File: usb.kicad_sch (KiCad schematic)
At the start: 11 parts, among them J7 USB-A_USB-303WSD-BRY, U1 AP22615AWU-7

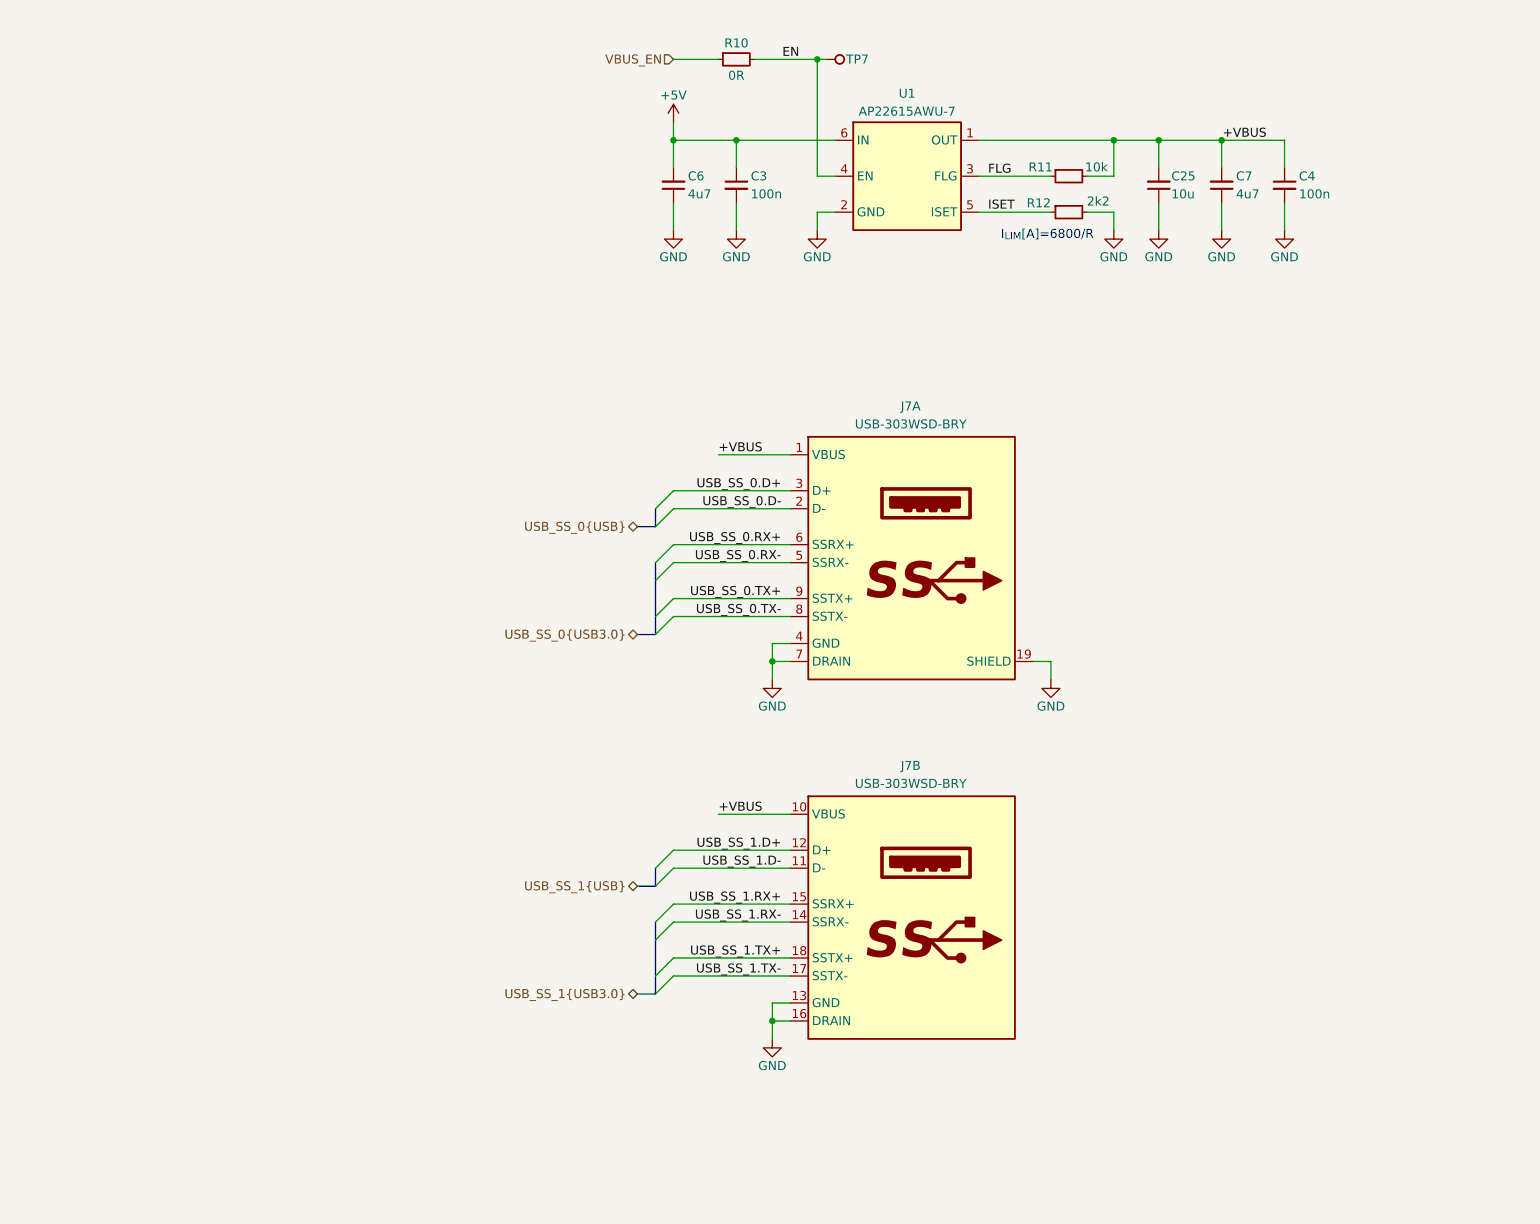
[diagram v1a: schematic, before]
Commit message: [#1] Add USB switch and 0R to USB hub data lines, minor schematic refactor
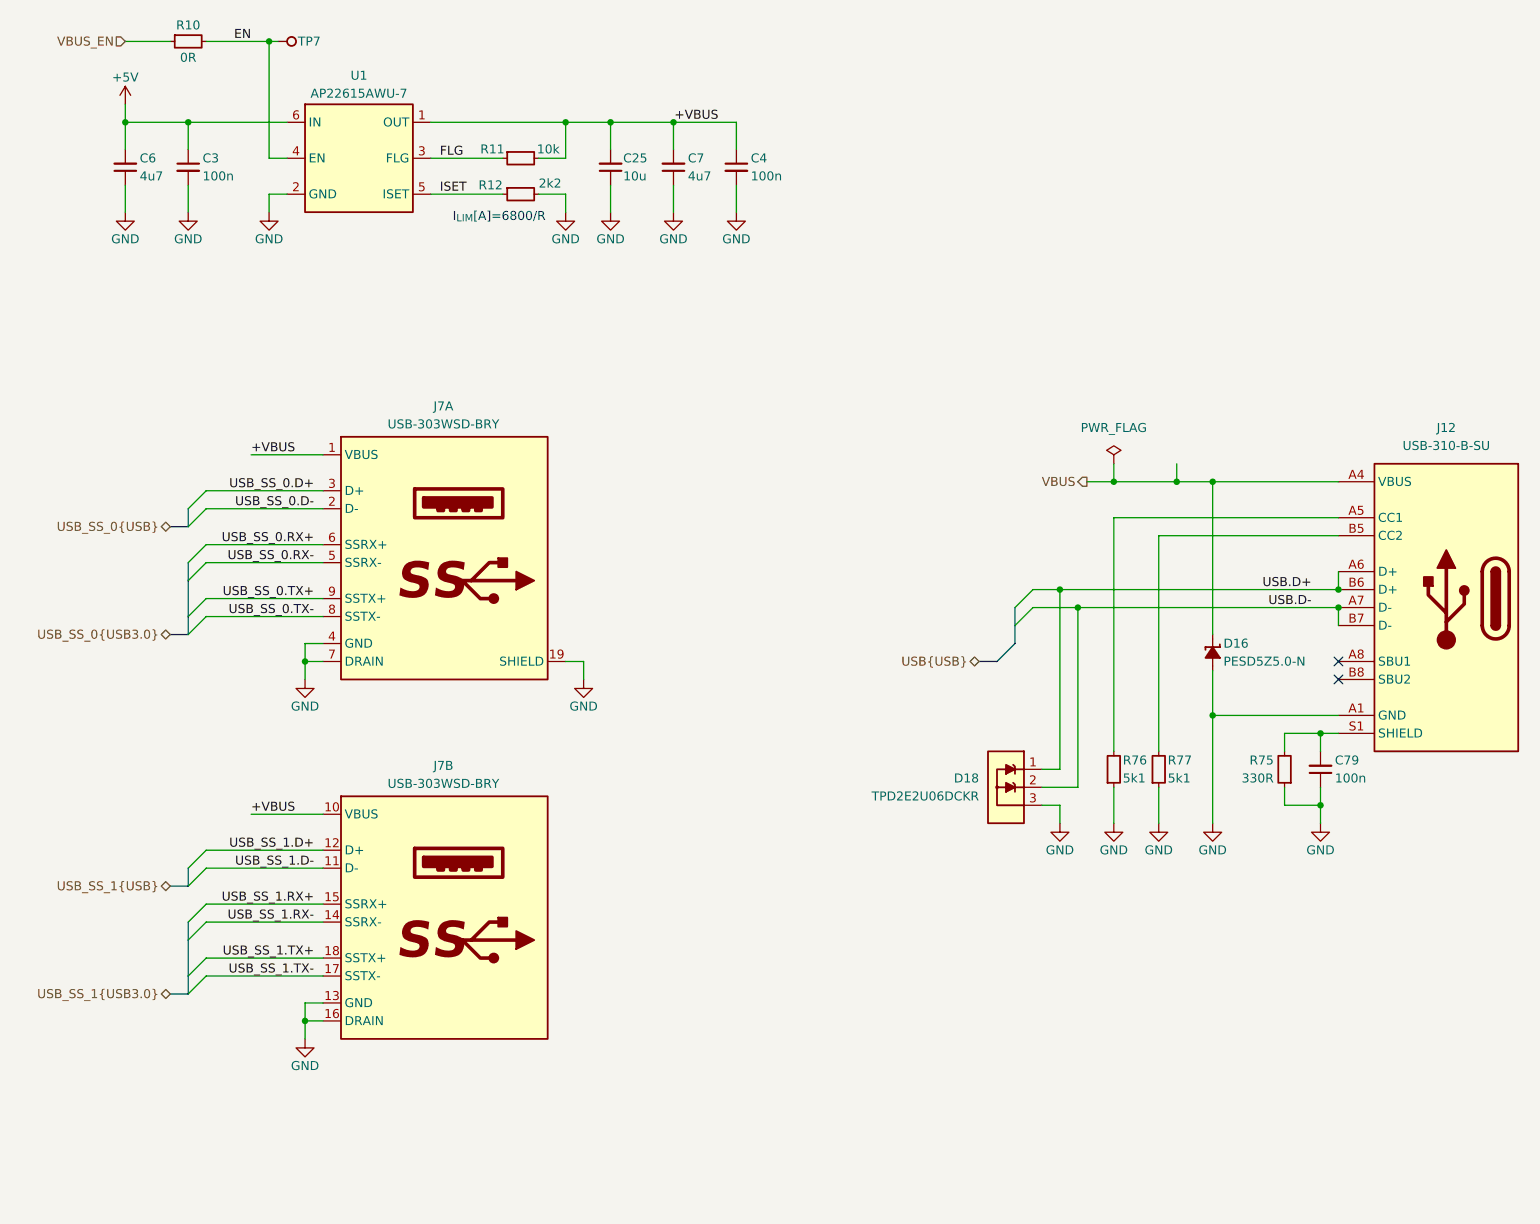
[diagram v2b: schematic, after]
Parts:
- added C79: C-100n-0402, DW-footprints:C_0402_1005Metric, symbol DW-capacitors:C-100n-0402
- added D16: PESD5Z5, DW-footprints:D_SOD-523, symbol DW-TVS:PESD5Z5
- added D18: TPD2E2U06DCKR, DW-footprints:SOT-323, symbol DW-TVS:TPD2E2U06DCKR
- added J12: USB-C_USB-310F-B-SU, DW-footprints:USB-C-Receptacle_USB-310-B-SU, symbol DW-connectors:USB-C_USB-310-B-SU
- added R75: R-330r-0402, DW-footprints:R_0402_1005Metric, symbol DW-resistors:R-330r-0402
- added R76, R77: R-5k1-0402, DW-footprints:R_0402_1005Metric, symbol DW-resistors:R-5k1-0402
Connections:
- net GND: now also C79.1, D16.2 (A), D18.3, J12.A1 (GND), J12.A12 (GND), J12.B1 (GND), J12.B12 (GND), R75.1, R76.1, R77.1
- new net: J12.A5 (CC1), R76.2
- new net: C79.2, J12.S1 (SHIELD), R75.2
- new net: J12.B5 (CC2), R77.2
- new net USB.D+: D18.1, J12.A6 (D+), J12.B6 (D+)
- new net USB.D-: D18.2, J12.A7 (D-), J12.B7 (D-)
- new net VBUS: D16.1 (C), J12.A4 (VBUS), J12.A9 (VBUS), J12.B4 (VBUS), J12.B9 (VBUS)
- no-connect marks 0 -> 2
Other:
- moved on the sheet: C25, C3, C4, C6, C7, J7A, J7B, R10, R11, R12, TP7, U1

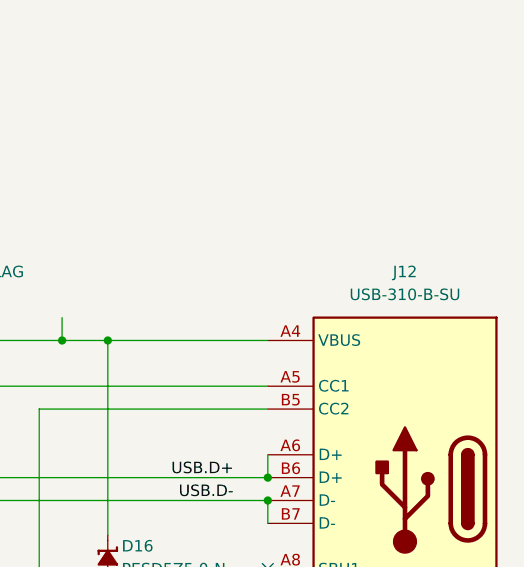
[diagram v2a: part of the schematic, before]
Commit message: [#3] Fix 3V3 DC-DC converter schematic, change one USB-C to a vertical one, start layout
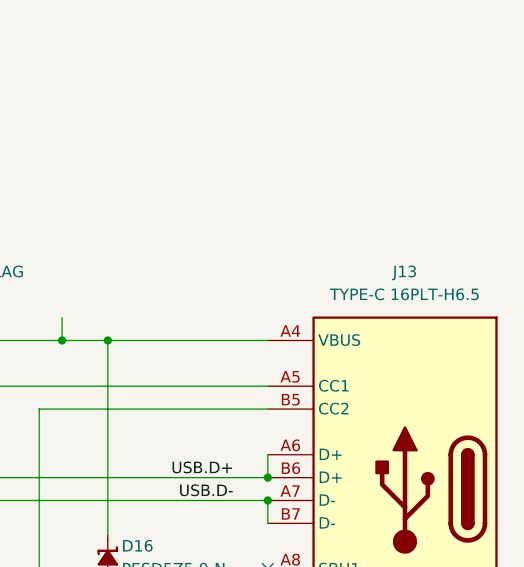
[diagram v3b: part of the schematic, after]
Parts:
- removed J12: USB-C_USB-310F-B-SU, DW-footprints:USB-C-Receptacle_USB-310-B-SU, symbol DW-connectors:USB-C_USB-310-B-SU
- added J13: USB-C_TYPE-C_16PLT-H6.5, DW-footprints:USB-C-Receptacle_TYPE-C_16PLT-H6.5, symbol DW-connectors:USB-C_TYPE-C_16PLT-H6.5
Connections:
- net GND: now also J13.A1 (GND), J13.A12 (GND), J13.B1 (GND), J13.B12 (GND)
- net USB.D+: now also J13.A6 (D+), J13.B6 (D+)
- net USB.D-: now also J13.A7 (D-), J13.B7 (D-)
- net VBUS: now also J13.A4 (VBUS), J13.A9 (VBUS), J13.B4 (VBUS), J13.B9 (VBUS)
- net at R76.2: now also J13.A5 (CC1)
- net at C79.2, R75.2: now also J13.S1 (SHIELD)
- net at R77.2: now also J13.B5 (CC2)
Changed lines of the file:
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@@
 	)
 	(junction
-		(at 210.82 107.95)
+		(at 210.82 110.49)
 		(diameter 0)
 		(color 0 0 0 0)
@@
 	)
 	(junction
-		(at 210.82 110.49)
-		(diameter 0)
-		(color 0 0 0 0)
-	)
-	(junction
 		(at 187.96 92.71)
 		(diameter 0)
@@
 	)
 	(junction
+		(at 210.82 107.95)
+		(diameter 0)
+		(color 0 0 0 0)
+	)
+	(junction
 		(at 193.04 125.73)
 		(diameter 0)
@@
 	)
 	(symbol
+		(lib_id "DW-connectors:USB-C_TYPE-C_16PLT-H6.5")
+		(at 210.82 92.71 0)
+		(unit 1)
+		(exclude_from_sim no)
+		(in_bom yes)
+		(on_board yes)
+		(dnp no)
+		(fields_autoplaced yes)
+		(property "Reference" "J13"
+			(at 226.06 85.09 0)
+			(effects
+				(font
+					(size 1.27 1.27)
+					(thickness 0.15)
+				)
+			)
+		)
+		(property "Value" "USB-C_TYPE-C_16PLT-H6.5"
+			(at 238.76 95.25 0)
+			(effects
+				(font
+					(size 1.27 1.27)
+					(thickness 0.15)
+				)
+				(justify left bottom)
+				(hide yes)
+			)
+		)
+		(property "Footprint" "DW-footprints:USB-C-Receptacle_TYPE-C_16PLT-H6.5"
+			(at 238.76 97.79 0)
+			(effects
+				(font
+					(size 1.27 1.27)
+					(thickness 0.15)
+				)
+				(justify left bottom)
+				(hide yes)
+			)
+		)
+		(property "Datasheet" "https://www.lcsc.com/datasheet/C3151748.pdf"
+			(at 238.76 100.33 0)
+			(effects
+				(font
+					(size 1.27 1.27)
+					(thickness 0.15)
+				)
+				(justify left bottom)
+				(hide yes)
+			)
+		)
+		(property "Description" "USB 3.1 5A 1 Surface Mount,Vertical 16P Female -40℃~+85℃ Type-C SMD USB Connectors ROHS"
+			(at 238.76 102.87 0)
+			(effects
+				(font
+					(size 1.27 1.27)
+					(thickness 0.15)
+				)
+				(justify left bottom)
+				(hide yes)
+			)
+		)
+		(property "Manufacturer" "SHOU HAN"
+			(at 238.76 105.41 0)
+			(effects
+				(font
+					(size 1.27 1.27)
+					(thickness 0.15)
+				)
+				(justify left bottom)
+				(hide yes)
+			)
+		)
+		(property "MPN" "TYPE-C 16PLT-H6.5"
+			(at 226.06 87.63 0)
+			(effects
+				(font
+					(size 1.27 1.27)
+					(thickness 0.15)
+				)
+			)
+		)
+		(property "LCSC" "C3151748"
+			(at 238.76 110.49 0)
+			(effects
+				(font
+					(size 1.27 1.27)
+					(thickness 0.15)
+				)
+				(justify left bottom)
+				(hide yes)
+			)
+		)
+		(pin "A9"
+		)
+		(pin "A4"
+		)
+		(pin "A5"
+		)
+		(pin "B7"
+		)
+		(pin "B8"
+		)
+		(pin "A8"
+		)
+		(pin "B5"
+		)
+		(pin "B6"
+		)
+		(pin "B1"
+		)
+		(pin "B12"
+		)
+		(pin "A7"
+		)
+		(pin "B4"
+		)
+		(pin "B9"
+		)
+		(pin "A1"
+		)
+		(pin "A12"
+		)
+		(pin "S1"
+		)
+		(pin "A6"
+		)
+		(instances
+			(project ""
+				(path "/090a8e41-87a8-4fb1-998b-60a2c0dc4cee/658b004a-eb7c-4ad1-a8df-d1cd97b62092"
+					(reference "J13")
+					(unit 1)
+				)
+			)
+		)
+	)
+	(symbol
 		(lib_id "DW-resistors:R-2k2-0402")
 		(at 92.71 52.07 0)
@@
 					(unit 1)
 				)
-			)
-		)
-	)
-	(symbol
-		(lib_id "DW-connectors:USB-C_USB-310-B-SU")
-		(at 210.82 92.71 0)
-		(unit 1)
-		(exclude_from_sim no)
-		(in_bom yes)
-		(on_board yes)
-		(dnp no)
-		(fields_autoplaced yes)
-		(property "Reference" "J12"
-			(at 226.06 85.09 0)
-			(effects
-				(font
-					(size 1.27 1.27)
-					(thickness 0.15)
-				)
-			)
-		)
-		(property "Value" "USB-C_USB-310F-B-SU"
-			(at 238.76 95.25 0)
-			(effects
-				(font
-					(size 1.27 1.27)
-					(thickness 0.15)
-				)
-				(justify left bottom)
-				(hide yes)
-			)
-		)
-		(property "Footprint" "DW-footprints:USB-C-Receptacle_USB-310-B-SU"
-			(at 238.76 97.79 0)
-			(effects
-				(font
-					(size 1.27 1.27)
-					(thickness 0.15)
-				)
-				(justify left bottom)
-				(hide yes)
-			)
-		)
-		(property "Datasheet" "https://lcsc.com/datasheet/lcsc_datasheet_2410122028_HOOYA-USB-310-B-SU_C309347.pdf"
-			(at 238.76 100.33 0)
-			(effects
-				(font
-					(size 1.27 1.27)
-					(thickness 0.15)
-				)
-				(justify left bottom)
-				(hide yes)
-			)
-		)
-		(property "Description" "3A 1 Surface Mount, Right Angle Female -20℃~+60℃ Type-C SMD USB Connectors ROHS"
-			(at 238.76 102.87 0)
-			(effects
-				(font
-					(size 1.27 1.27)
-					(thickness 0.15)
-				)
-				(justify left bottom)
-				(hide yes)
-			)
-		)
-		(property "Manufacturer" "HOOYA"
-			(at 238.76 105.41 0)
-			(effects
-				(font
-					(size 1.27 1.27)
-					(thickness 0.15)
-				)
-				(justify left bottom)
-				(hide yes)
-			)
-		)
-		(property "MPN" "USB-310-B-SU"
-			(at 226.06 87.63 0)
-			(effects
-				(font
-					(size 1.27 1.27)
-					(thickness 0.15)
-				)
-			)
-		)
-		(property "LCSC" "C309347"
-			(at 238.76 110.49 0)
-			(effects
-				(font
-					(size 1.27 1.27)
-					(thickness 0.15)
-				)
-				(justify left bottom)
-				(hide yes)
-			)
-		)
-		(pin "A7"
-		)
-		(pin "B7"
-		)
-		(pin "B6"
-		)
-		(pin "B4"
-		)
-		(pin "A8"
-		)
-		(pin "B8"
-		)
-		(pin "A1"
-		)
-		(pin "A5"
-		)
-		(pin "B12"
-		)
-		(pin "B1"
-		)
-		(pin "A12"
-		)
-		(pin "S1"
-		)
-		(pin "A4"
-		)
-		(pin "A9"
-		)
-		(pin "B9"
-		)
-		(pin "B5"
-		)
-		(pin "A6"
-		)
-		(instances
-			(project "cm5-module"
-				(path "/090a8e41-87a8-4fb1-998b-60a2c0dc4cee/658b004a-eb7c-4ad1-a8df-d1cd97b62092"
-					(reference "J12")
-					(unit 1)
-				)
